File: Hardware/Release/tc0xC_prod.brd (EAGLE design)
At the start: 98.6 x 99.6 mm, 108 parts, among them IC1 AP2112M-3.3TRG1, Q1 2.5A/30V, Q2 MBT3904DW1T1, Q3 600mA/40V, Q4 MBT3904DW1T1, U2 ESP3212, U4 FT231XS, U5 W25Q32FVSS, Y1 26MHz, Y2 32.768kHz

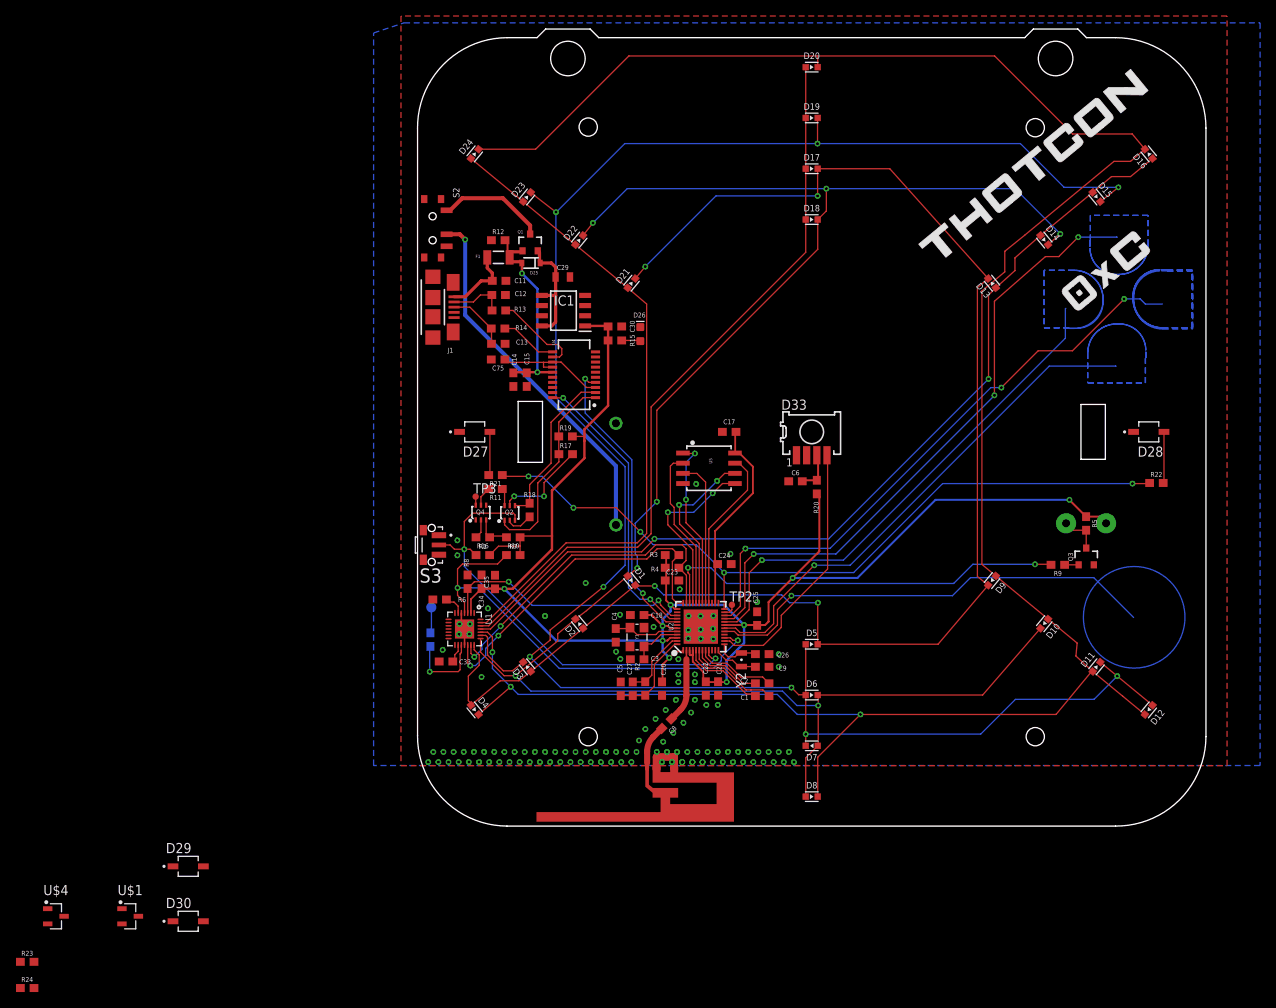
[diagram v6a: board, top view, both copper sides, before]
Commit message: Hardware and Art dirs
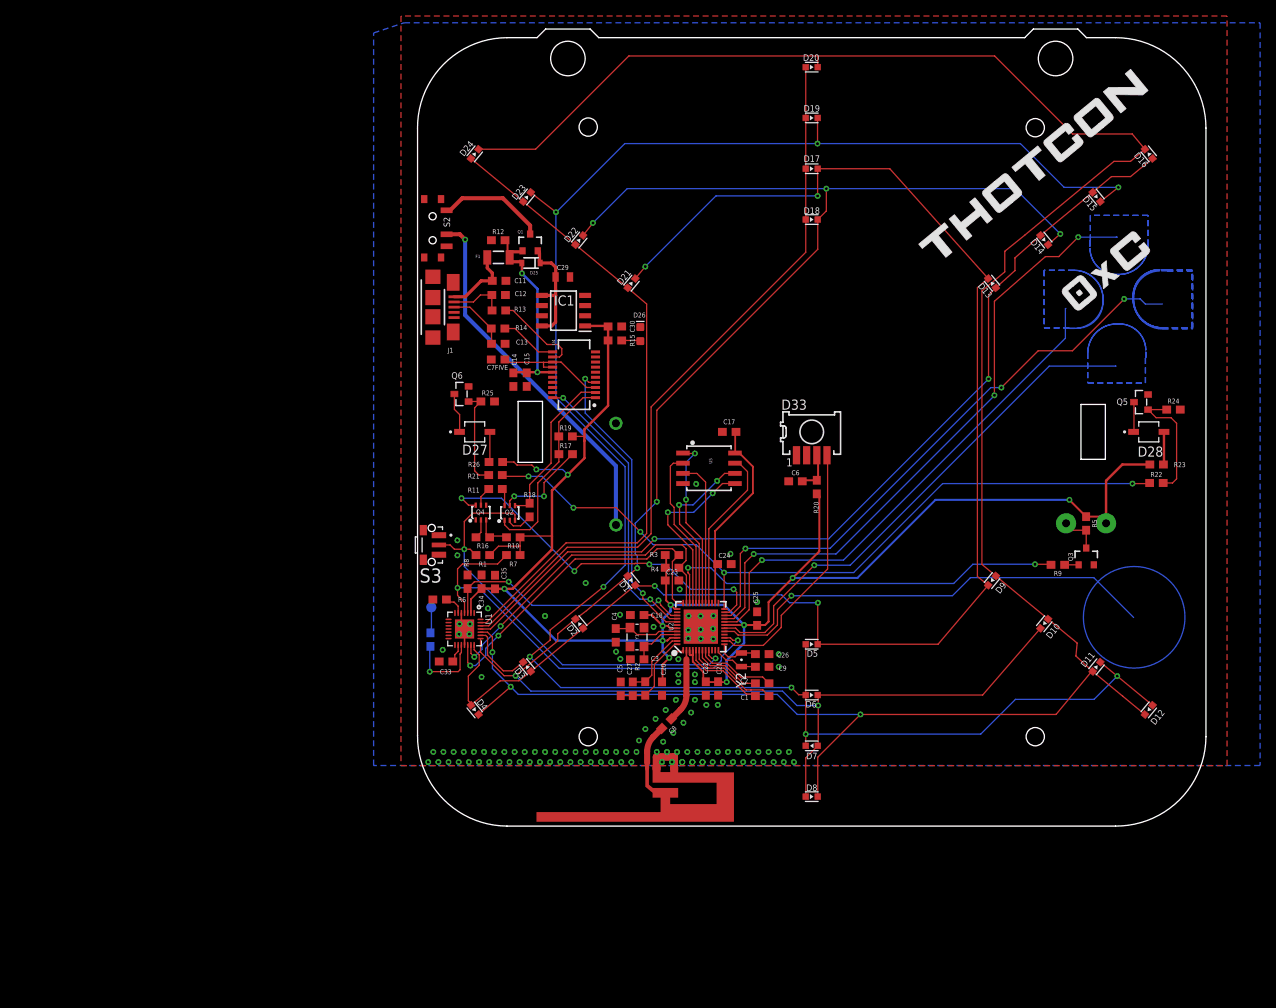
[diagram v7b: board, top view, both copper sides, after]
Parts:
- removed D29, D30: VSMB2020X01, VSMB2020X01:DIO_VSMB2020X01
- removed TP2, TP3: TPSTP08R, testpad:TP08R
- removed U$1, U$4: T2N7002BK, T2N7002BK:SOT-23/E0-95/B0-4
- added Q5, Q6: MOSFET-NCH-RUC002N05HZGT116, Rob-DiscreteSemi:SOT-23-3
- added R25: 100K, SparkFun-Resistors:0603
- added R26: 22, SparkFun-Resistors:0603
- R22: value 8.2 -> 240
- R23: value 8.2 -> 22
- R24: value 8.2 -> 100K
- moved R24 160.5 mm to (96.0, 53.6)
- moved R23 154.3 mm to (93.9, 46.7)
- renumbered C75 to C7FIVE
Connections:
- removed net T_B1: TP2.TP, U2.23
- removed net T_B2: Q4.6, TP3.TP
- new net GPIO-0: Q4.6, U2.23
- net 3.3V: now also R26.1; no longer R24.1
- net GND: now also Q5.2, Q6.2, R24.2, R25.2; no longer D27.C, D28.C, U$1.2, U$4.2
- net IR_OUT: no longer U$1.1, U$4.1
- net N$19: now also D28.C, Q5.3; no longer D29.C, U$1.3
- net N$20: now also D28.A, R23.2; no longer D30.C, U$4.3
- net N$21: now also D27.C, Q6.3; no longer D29.A, R23.2
- net N$22: now also D27.A, R26.2; no longer D30.A, R24.2
- net N$5: now also Q6.1, R25.1; no longer D27.A
- net N$6: now also Q5.1, R24.1; no longer D28.A
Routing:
- net GPIO-0: track 0.00 -> 45.8 mm, vias 0 -> 4
- net 3.3V: track 206.9 -> 227.3 mm, vias 9 -> 11
- net N$6: track 6.43 -> 15.4 mm
- net N$5: track 5.46 -> 12.5 mm
- net N$21: track 0.00 -> 5.01 mm
- net N$20: track 0.00 -> 4.11 mm
- net N$22: track 0.00 -> 3.81 mm
- net N$19: track 0.00 -> 3.74 mm
- net T_B1: track 1.69 -> 0.00 mm
- net T_B2: track 1.08 -> 0.00 mm
